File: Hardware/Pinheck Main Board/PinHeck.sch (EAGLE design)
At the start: 363 parts, among them IC2 PIC32MX795F512L-80I/PT, IC3 CD74HCT244E, IC4 CD74HCT244E, IC5 ULN2803A, J11 TC2030-FTDI-TTL-232R, J2 TC2030-FTDI-TTL-232R, J3 N/A, J4 SJ1-2503A, J5 26-64-4020, J9 TC2030-PKT-NL, P1 TC33X-2-103E, U1 P8X32A-Q44, U10 74HCT2G04GV,125, U11 CD74HC165M96, U12 CD74HC165M96, U13 CAT24M01LI-G, U14 MC74HC08ADR2G, U15 MC74HC08ADR2G, U16 MC74HC08ADR2G, U17 MC74HC08ADR2G, U18 MC74HC08ADR2G, U19 MC74HC08ADR2G, U2 DS1340Z-33+, U20 TIP107, U21 TIP107, U22 TIP107, U23 TIP107, U24 TIP107, U25 TIP107, U26 TIP107, U27 TIP107, U28 TIP102, U29 TIP102, U3 CD74HC595M96, U30 TIP102, U31 TIP102, U32 TIP102, U33 TIP102, U34 TIP102, U35 TIP102, U36 WS2801, U37 TIP102, U38 WS2801, U39 NCP1117DT33G, U4 CAT24M01LI-G, U40 TIP102, U41 TIP102, U42 TIP102, U43 TIP102, U44 TIP102, U45 TIP102, U46 TIP102, U47 TIP102, U48 TIP102, U49 TIP102, U5 CD74HC595M96, U50 TIP102, U51 TIP102, U52 CD74HC123M96, U6 TIP102, U7 TIP102, U8 TIP102, U9 TIP102, X1 FQ7050B-8.000, X2 9C-6.500MAAJ-T, X3 ABS25-32.768KHz-1-T

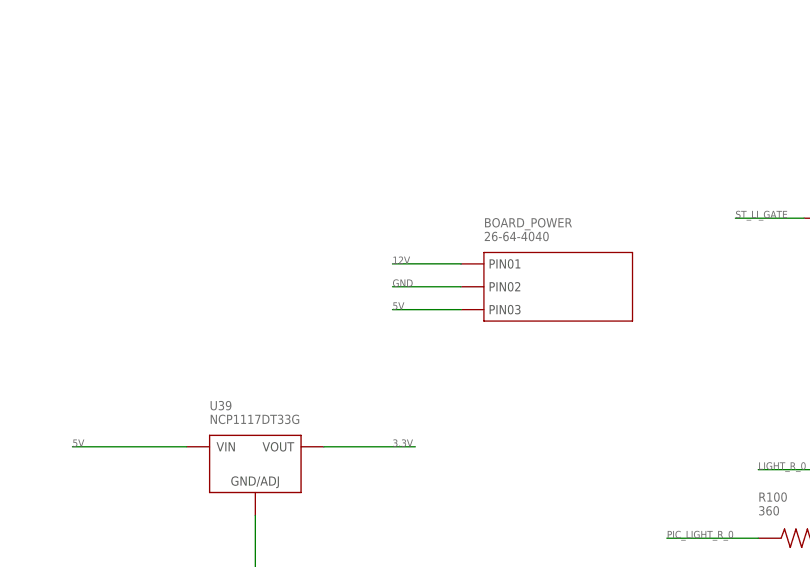
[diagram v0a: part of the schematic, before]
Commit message: Starting layout of parts and connectors
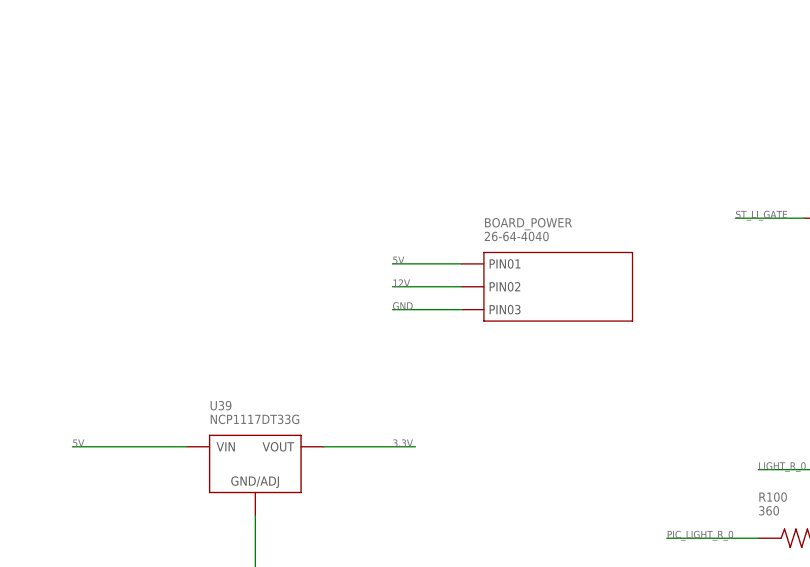
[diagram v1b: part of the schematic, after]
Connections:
- net 12V: now also BOARD_POWER.PIN2; no longer BOARD_POWER.PIN1
- net 5V: now also BOARD_POWER.PIN1; no longer BOARD_POWER.PIN3
- net GND: now also BOARD_POWER.PIN3; no longer BOARD_POWER.PIN2
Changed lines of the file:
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@@
 <grid distance="0.1" unitdist="inch" unit="inch" style="lines" multiple="1" display="no" altdistance="0.01" altunitdist="inch" altunit="inch"/>
 <layers>
-<layer number="1" name="Top" color="4" fill="1" visible="yes" active="no"/>
-<layer number="2" name="Route2" color="1" fill="3" visible="yes" active="no"/>
-<layer number="3" name="Route3" color="4" fill="3" visible="yes" active="no"/>
-<layer number="4" name="Route4" color="1" fill="4" visible="yes" active="no"/>
-<layer number="5" name="Route5" color="4" fill="4" visible="yes" active="no"/>
-<layer number="6" name="Route6" color="1" fill="8" visible="yes" active="no"/>
-<layer number="7" name="Route7" color="4" fill="8" visible="yes" active="no"/>
-<layer number="8" name="Route8" color="1" fill="2" visible="yes" active="no"/>
-<layer number="9" name="Route9" color="4" fill="2" visible="yes" active="no"/>
-<layer number="10" name="Route10" color="1" fill="7" visible="yes" active="no"/>
-<layer number="11" name="Route11" color="4" fill="7" visible="yes" active="no"/>
-<layer number="12" name="Route12" color="1" fill="5" visible="yes" active="no"/>
-<layer number="13" name="Route13" color="4" fill="5" visible="yes" active="no"/>
-<layer number="14" name="Route14" color="1" fill="6" visible="yes" active="no"/>
-<layer number="15" name="Route15" color="4" fill="6" visible="yes" active="no"/>
-<layer number="16" name="Bottom" color="1" fill="1" visible="yes" active="no"/>
-<layer number="17" name="Pads" color="2" fill="1" visible="yes" active="no"/>
-<layer number="18" name="Vias" color="2" fill="1" visible="yes" active="no"/>
-<layer number="19" name="Unrouted" color="6" fill="1" visible="yes" active="no"/>
-<layer number="20" name="Dimension" color="15" fill="1" visible="yes" active="no"/>
-<layer number="21" name="tPlace" color="7" fill="1" visible="yes" active="no"/>
-<layer number="22" name="bPlace" color="7" fill="1" visible="yes" active="no"/>
-<layer number="23" name="tOrigins" color="15" fill="1" visible="yes" active="no"/>
-<layer number="24" name="bOrigins" color="15" fill="1" visible="yes" active="no"/>
-<layer number="25" name="tNames" color="7" fill="1" visible="yes" active="no"/>
-<layer number="26" name="bNames" color="7" fill="1" visible="yes" active="no"/>
-<layer number="27" name="tValues" color="7" fill="1" visible="yes" active="no"/>
-<layer number="28" name="bValues" color="7" fill="1" visible="yes" active="no"/>
+<layer number="1" name="Top" color="4" fill="1" visible="no" active="no"/>
+<layer number="2" name="Route2" color="1" fill="3" visible="no" active="no"/>
+<layer number="3" name="Route3" color="4" fill="3" visible="no" active="no"/>
+<layer number="4" name="Route4" color="1" fill="4" visible="no" active="no"/>
+<layer number="5" name="Route5" color="4" fill="4" visible="no" active="no"/>
+<layer number="6" name="Route6" color="1" fill="8" visible="no" active="no"/>
+<layer number="7" name="Route7" color="4" fill="8" visible="no" active="no"/>
+<layer number="8" name="Route8" color="1" fill="2" visible="no" active="no"/>
+<layer number="9" name="Route9" color="4" fill="2" visible="no" active="no"/>
+<layer number="10" name="Route10" color="1" fill="7" visible="no" active="no"/>
+<layer number="11" name="Route11" color="4" fill="7" visible="no" active="no"/>
+<layer number="12" name="Route12" color="1" fill="5" visible="no" active="no"/>
+<layer number="13" name="Route13" color="4" fill="5" visible="no" active="no"/>
+<layer number="14" name="Route14" color="1" fill="6" visible="no" active="no"/>
+<layer number="15" name="Route15" color="4" fill="6" visible="no" active="no"/>
+<layer number="16" name="Bottom" color="1" fill="1" visible="no" active="no"/>
+<layer number="17" name="Pads" color="2" fill="1" visible="no" active="no"/>
+<layer number="18" name="Vias" color="2" fill="1" visible="no" active="no"/>
+<layer number="19" name="Unrouted" color="6" fill="1" visible="no" active="no"/>
+<layer number="20" name="Dimension" color="15" fill="1" visible="no" active="no"/>
+<layer number="21" name="tPlace" color="7" fill="1" visible="no" active="no"/>
+<layer number="22" name="bPlace" color="7" fill="1" visible="no" active="no"/>
+<layer number="23" name="tOrigins" color="15" fill="1" visible="no" active="no"/>
+<layer number="24" name="bOrigins" color="15" fill="1" visible="no" active="no"/>
+<layer number="25" name="tNames" color="7" fill="1" visible="no" active="no"/>
+<layer number="26" name="bNames" color="7" fill="1" visible="no" active="no"/>
+<layer number="27" name="tValues" color="7" fill="1" visible="no" active="no"/>
+<layer number="28" name="bValues" color="7" fill="1" visible="no" active="no"/>
 <layer number="29" name="tStop" color="7" fill="3" visible="no" active="no"/>
 <layer number="30" name="bStop" color="7" fill="6" visible="no" active="no"/>
@@
 <layer number="35" name="tGlue" color="7" fill="4" visible="no" active="no"/>
 <layer number="36" name="bGlue" color="7" fill="5" visible="no" active="no"/>
-<layer number="37" name="tTest" color="7" fill="1" visible="yes" active="no"/>
-<layer number="38" name="bTest" color="7" fill="1" visible="yes" active="no"/>
+<layer number="37" name="tTest" color="7" fill="1" visible="no" active="no"/>
+<layer number="38" name="bTest" color="7" fill="1" visible="no" active="no"/>
 <layer number="39" name="tKeepout" color="4" fill="11" visible="no" active="no"/>
 <layer number="40" name="bKeepout" color="1" fill="11" visible="no" active="no"/>
@@
 <layer number="44" name="Drills" color="7" fill="1" visible="no" active="no"/>
 <layer number="45" name="Holes" color="7" fill="1" visible="no" active="no"/>
-<layer number="46" name="Milling" color="3" fill="1" visible="yes" active="no"/>
-<layer number="47" name="Measures" color="7" fill="1" visible="yes" active="no"/>
-<layer number="48" name="Document" color="7" fill="1" visible="yes" active="no"/>
-<layer number="49" name="Reference" color="7" fill="1" visible="yes" active="no"/>
-<layer number="50" name="dxf" color="7" fill="1" visible="yes" active="no"/>
-<layer number="51" name="tDocu" color="7" fill="1" visible="yes" active="no"/>
-<layer number="52" name="bDocu" color="7" fill="1" visible="yes" active="no"/>
-<layer number="53" name="tGND_GNDA" color="7" fill="9" visible="yes" active="no"/>
-<layer number="54" name="bGND_GNDA" color="1" fill="9" visible="yes" active="no"/>
-<layer number="56" name="wert" color="7" fill="1" visible="yes" active="no"/>
+<layer number="46" name="Milling" color="3" fill="1" visible="no" active="no"/>
+<layer number="47" name="Measures" color="7" fill="1" visible="no" active="no"/>
+<layer number="48" name="Document" color="7" fill="1" visible="no" active="no"/>
+<layer number="49" name="Reference" color="7" fill="1" visible="no" active="no"/>
+<layer number="50" name="dxf" color="7" fill="1" visible="no" active="no"/>
+<layer number="51" name="tDocu" color="7" fill="1" visible="no" active="no"/>
+<layer number="52" name="bDocu" color="7" fill="1" visible="no" active="no"/>
+<layer number="53" name="tGND_GNDA" color="7" fill="9" visible="no" active="no"/>
+<layer number="54" name="bGND_GNDA" color="1" fill="9" visible="no" active="no"/>
+<layer number="56" name="wert" color="7" fill="1" visible="no" active="no"/>
 <layer number="91" name="Nets" color="2" fill="1" visible="yes" active="yes"/>
 <layer number="92" name="Busses" color="1" fill="1" visible="yes" active="yes"/>
@@
 </segment>
 <segment>
-<wire x1="795.02" y1="182.88" x2="787.4" y2="182.88" width="0.1524" layer="91"/>
-<label x="787.4" y="182.88" size="0.8128" layer="95" font="vector"/>
-<pinref part="BOARD_POWER" gate="G$1" pin="PIN2"/>
-</segment>
-<segment>
 <wire x1="525.78" y1="5.08" x2="518.16" y2="5.08" width="0.1524" layer="91"/>
 <pinref part="C48" gate="G$1" pin="2"/>
@@
 <label x="678.18" y="-73.66" size="0.8128" layer="95" font="vector"/>
 </segment>
+<segment>
+<wire x1="795.02" y1="180.34" x2="787.4" y2="180.34" width="0.1524" layer="91"/>
+<label x="787.4" y="180.34" size="0.8128" layer="95" font="vector"/>
+<pinref part="BOARD_POWER" gate="G$1" pin="PIN3"/>
+</segment>
 </net>
 <net name="RX_PIC32" class="0">
@@
 </segment>
 <segment>
-<wire x1="795.02" y1="180.34" x2="787.4" y2="180.34" width="0.1524" layer="91"/>
-<label x="787.4" y="180.34" size="0.8128" layer="95" font="vector"/>
-<pinref part="BOARD_POWER" gate="G$1" pin="PIN3"/>
-</segment>
-<segment>
 <wire x1="525.78" y1="17.78" x2="518.16" y2="17.78" width="0.1524" layer="91"/>
 <pinref part="C48" gate="G$1" pin="1"/>
@@
 <label x="688.34" y="-58.42" size="0.8128" layer="95" font="vector"/>
 </segment>
+<segment>
+<wire x1="795.02" y1="185.42" x2="787.4" y2="185.42" width="0.1524" layer="91"/>
+<label x="787.4" y="185.42" size="0.8128" layer="95" font="vector"/>
+<pinref part="BOARD_POWER" gate="G$1" pin="PIN1"/>
+</segment>
 </net>
 <net name="DATA_LAT" class="0">
@@
 </segment>
 <segment>
-<wire x1="795.02" y1="185.42" x2="787.4" y2="185.42" width="0.1524" layer="91"/>
-<label x="787.4" y="185.42" size="0.8128" layer="95" font="vector"/>
-<pinref part="BOARD_POWER" gate="G$1" pin="PIN1"/>
-</segment>
-<segment>
 <pinref part="J7" gate="G$1" pin="PIN1"/>
 <wire x1="914.4" y1="40.64" x2="901.7" y2="40.64" width="0.1524" layer="91"/>
 <label x="901.7" y="40.64" size="0.8128" layer="95" font="vector"/>
 </segment>
+<segment>
+<wire x1="795.02" y1="182.88" x2="787.4" y2="182.88" width="0.1524" layer="91"/>
+<label x="787.4" y="182.88" size="0.8128" layer="95" font="vector"/>
+<pinref part="BOARD_POWER" gate="G$1" pin="PIN2"/>
+</segment>
 </net>

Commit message: Layout of parts almost done. Needs some tweaking but everything fits.
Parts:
- PIC32_UART: LABEL01 (none) -> GND; LABEL04 (none) -> RX_PIC32; LABEL05 (none) -> TX_PIC32; LABEL06 (none) -> !RST!_PIC32
- PROP_UART: LABEL01 (none) -> GND; LABEL04 (none) -> RX_PROP; LABEL05 (none) -> TX_PROP; LABEL06 (none) -> !RES!_PROP
- renumbered J1 to PROP_UART, J10 to PIC32_UART, J11 to PIC32_TC, J2 to PROP_TC, J8 to PICKIT3, J9 to PICKIT3_TC, SW1 to PIC_RST, SW3 to PIC_PROGRAM

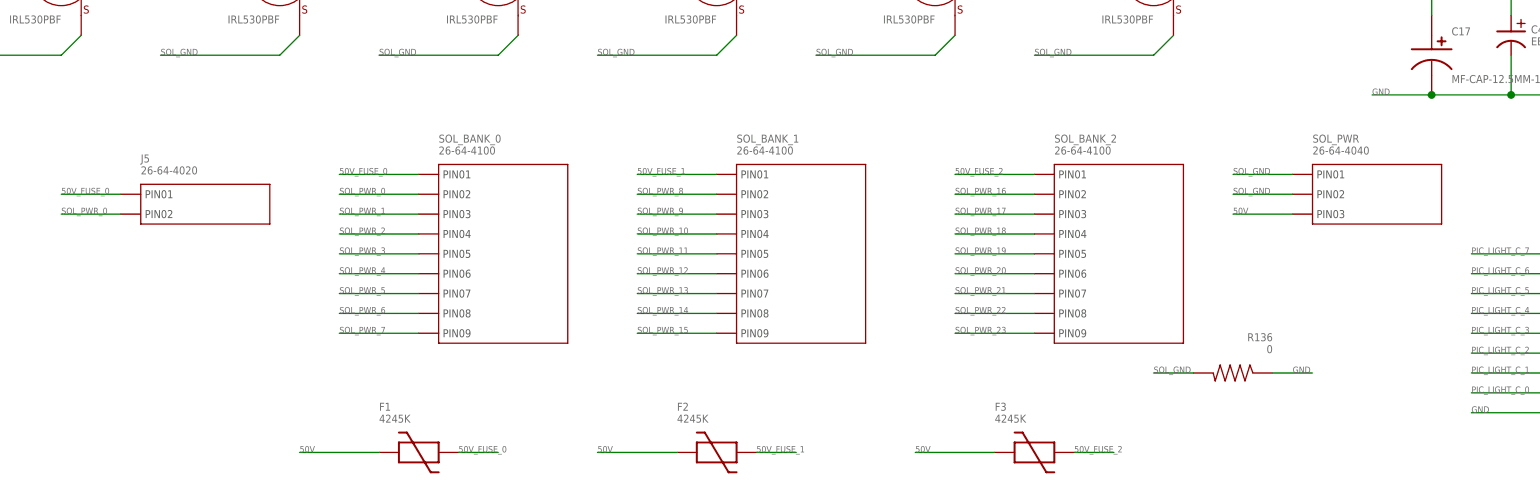
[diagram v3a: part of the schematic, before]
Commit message: Routing the solenoid power area.
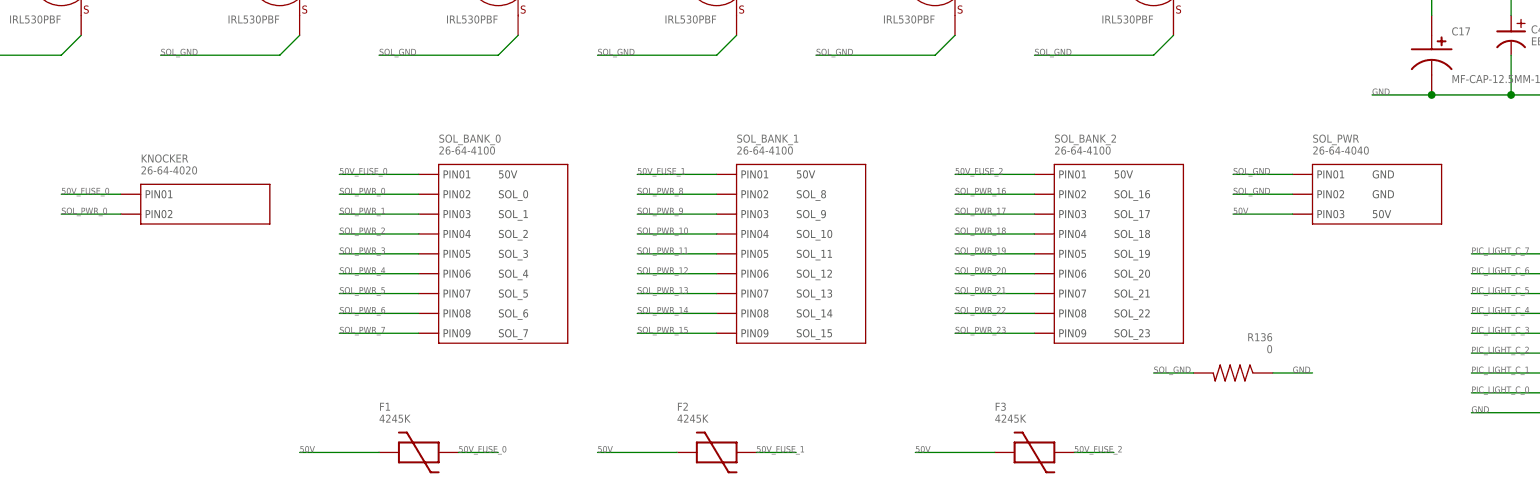
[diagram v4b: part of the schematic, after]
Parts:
- SOL_BANK_0: LABEL01 (none) -> 50V; LABEL02 (none) -> SOL_0; LABEL03 (none) -> SOL_1; LABEL04 (none) -> SOL_2; LABEL05 (none) -> SOL_3; LABEL06 (none) -> SOL_4; LABEL07 (none) -> SOL_5; LABEL08 (none) -> SOL_6; LABEL09 (none) -> SOL_7
- SOL_BANK_1: LABEL01 (none) -> 50V; LABEL02 (none) -> SOL_8; LABEL03 (none) -> SOL_9; LABEL04 (none) -> SOL_10; LABEL05 (none) -> SOL_11; LABEL06 (none) -> SOL_12; LABEL07 (none) -> SOL_13; LABEL08 (none) -> SOL_14; LABEL09 (none) -> SOL_15
- SOL_BANK_2: LABEL01 (none) -> 50V; LABEL02 (none) -> SOL_16; LABEL03 (none) -> SOL_17; LABEL04 (none) -> SOL_18; LABEL05 (none) -> SOL_19; LABEL06 (none) -> SOL_20; LABEL07 (none) -> SOL_21; LABEL08 (none) -> SOL_22; LABEL09 (none) -> SOL_23
- SOL_PWR: LABEL01 (none) -> GND; LABEL02 (none) -> GND; LABEL03 (none) -> 50V
- renumbered J5 to KNOCKER
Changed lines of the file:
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@@
 <part name="R137" library="PP_Passives" deviceset="RESISTOR" device="_0805" value="10K"/>
 <part name="U$2" library="PP_Aesthetics" deviceset="MF_LOGO" device="LOGO_TEXT"/>
-<part name="SOL_BANK_0" library="PP_Connectors" deviceset="CON_01X09" device="_26-64-4100_(KEYPIN6)" value="26-64-4100"/>
-<part name="SOL_BANK_1" library="PP_Connectors" deviceset="CON_01X09" device="_26-64-4100_(KEYPIN7)" value="26-64-4100"/>
-<part name="SOL_BANK_2" library="PP_Connectors" deviceset="CON_01X09" device="_26-64-4100_(KEYPIN8)" value="26-64-4100"/>
+<part name="SOL_BANK_0" library="PP_Connectors" deviceset="CON_01X09" device="_26-64-4100_(KEYPIN6)" value="26-64-4100">
+<attribute name="LABEL01" value="50V"/>
+<attribute name="LABEL02" value="SOL_0"/>
+<attribute name="LABEL03" value="SOL_1"/>
+<attribute name="LABEL04" value="SOL_2"/>
+<attribute name="LABEL05" value="SOL_3"/>
+<attribute name="LABEL06" value="SOL_4"/>
+<attribute name="LABEL07" value="SOL_5"/>
+<attribute name="LABEL08" value="SOL_6"/>
+<attribute name="LABEL09" value="SOL_7"/>
+</part>
+<part name="SOL_BANK_1" library="PP_Connectors" deviceset="CON_01X09" device="_26-64-4100_(KEYPIN7)" value="26-64-4100">
+<attribute name="LABEL01" value="50V"/>
+<attribute name="LABEL02" value="SOL_8"/>
+<attribute name="LABEL03" value="SOL_9"/>
+<attribute name="LABEL04" value="SOL_10"/>
+<attribute name="LABEL05" value="SOL_11"/>
+<attribute name="LABEL06" value="SOL_12"/>
+<attribute name="LABEL07" value="SOL_13"/>
+<attribute name="LABEL08" value="SOL_14"/>
+<attribute name="LABEL09" value="SOL_15"/>
+</part>
+<part name="SOL_BANK_2" library="PP_Connectors" deviceset="CON_01X09" device="_26-64-4100_(KEYPIN8)" value="26-64-4100">
+<attribute name="LABEL01" value="50V"/>
+<attribute name="LABEL02" value="SOL_16"/>
+<attribute name="LABEL03" value="SOL_17"/>
+<attribute name="LABEL04" value="SOL_18"/>
+<attribute name="LABEL05" value="SOL_19"/>
+<attribute name="LABEL06" value="SOL_20"/>
+<attribute name="LABEL07" value="SOL_21"/>
+<attribute name="LABEL08" value="SOL_22"/>
+<attribute name="LABEL09" value="SOL_23"/>
+</part>
 <part name="SW_ROW" library="PP_Connectors" deviceset="CON_01X09" device="_26-64-4100_(KEYPIN4)" value="26-64-4100"/>
 <part name="SW_COL" library="PP_Connectors" deviceset="CON_01X09" device="_26-64-4100_(KEYPIN5)" value="26-64-4100"/>
@@
 <part name="U4" library="PP_DigitalIC" deviceset="EEPROM_I2C" device="DIP-8" value="CAT24M01LI-G"/>
 <part name="BOARD_POWER" library="PP_Connectors" deviceset="CON_01X03" device="_26-64-4040_(KEYPIN2)" value="26-64-4040"/>
-<part name="SOL_PWR" library="PP_Connectors" deviceset="CON_01X03" device="_26-64-4040_(KEYPIN3)" value="26-64-4040"/>
+<part name="SOL_PWR" library="PP_Connectors" deviceset="CON_01X03" device="_26-64-4040_(KEYPIN3)" value="26-64-4040">
+<attribute name="LABEL01" value="GND"/>
+<attribute name="LABEL02" value="GND"/>
+<attribute name="LABEL03" value="50V"/>
+</part>
 <part name="U1" library="PP_DigitalIC" deviceset="P8X32A" device="-Q44" value="P8X32A-Q44"/>
 <part name="DMD_CON" library="PP_Connectors" deviceset="CON_02X07" device="_5103308-2" value="5103308-2"/>
@@
 <part name="J7" library="PP_Connectors" deviceset="CON_01X03" device="_26-64-4040_(KEYPIN1)"/>
 <part name="CABINET" library="PP_Connectors" deviceset="CON_01X11" device="_26-64-4120(KEYPIN2)" value="26-64-4120"/>
-<part name="J5" library="PP_Connectors" deviceset="CON_01X02" device="_26-64-4020" value="26-64-4020"/>
+<part name="KNOCKER" library="PP_Connectors" deviceset="CON_01X02" device="_26-64-4020" value="26-64-4020"/>
 <part name="PICKIT3" library="PP_Connectors" deviceset="CON_01X06" device="_2.54MM_PIN_HEADER"/>
 <part name="R24" library="PP_Passives" deviceset="RESISTOR" device="_0805" value="10K"/>
@@
 <instance part="J7" gate="G$1" x="916.94" y="40.64"/>
 <instance part="CABINET" gate="G$1" x="518.16" y="86.36"/>
-<instance part="J5" gate="G$1" x="581.66" y="81.28"/>
+<instance part="KNOCKER" gate="G$1" x="581.66" y="81.28"/>
 <instance part="PICKIT3" gate="G$1" x="15.24" y="106.68"/>
 <instance part="R24" gate="G$1" x="350.52" y="213.36" rot="R90"/>
@@
 <wire x1="571.5" y1="81.28" x2="579.12" y2="81.28" width="0.1524" layer="91"/>
 <label x="571.5" y="81.28" size="0.8128" layer="95" font="vector"/>
-<pinref part="J5" gate="G$1" pin="PIN1"/>
+<pinref part="KNOCKER" gate="G$1" pin="PIN1"/>
 </segment>
 </net>
@@
 <wire x1="579.12" y1="78.74" x2="571.5" y2="78.74" width="0.1524" layer="91"/>
 <label x="571.5" y="78.74" size="0.8128" layer="95" font="vector"/>
-<pinref part="J5" gate="G$1" pin="PIN2"/>
+<pinref part="KNOCKER" gate="G$1" pin="PIN2"/>
 </segment>
 <segment>

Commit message: Added changes for Ben
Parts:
- U37: value TIP102 -> TIP107; device PP_DiscreteSemi:BJT_NPN_SINGLE_TO-220 -> PP_DiscreteSemi:BJT_PNP_SINGLE_TO-220
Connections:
- net AC_17 renamed SERVO_2
- net AC_33 renamed SERVO_4
- net AC_34 renamed SERVO_3
- net AC_44 renamed SERVO_1
- net AC_46 renamed SERVO_0
- net COMM_ATN renamed COMM_IN_TX
- net COMM_CLK renamed COMM_CLK_RX
- net COMM_DATA renamed COMM_OUT
- net DATA_CAB renamed CAB_SWITCH_IN
- net DATA_CLK renamed CAB_CLK
- net DATA_LAT renamed CAB_LAT
- net GI_DATA_COL renamed CAB_GI_OUT
- net MENU renamed BACK
- net RG9 renamed PIC_PROGRAM_SW
- removed net RC1: IC2PC.T2CK/RC1
- removed net RG6: IC2PG.ECOL/SCK2A/U2BTXU2ARTS/PMA5/CN8/RG6
- new net EXT_RGB_CLK: IC2PC.T2CK/RC1, RGB_COM_OUT.3
- new net EXT_RGB_DATA: IC2PG.ECOL/SCK2A/U2BTXU2ARTS/PMA5/CN8/RG6, RGB_COM_OUT.2
- net 5V: now also R115.1, U37.EMITTER
- net GND: no longer R115.1, U37.EMITTER
- net RGB_CLK_OUT: no longer RGB_COM_OUT.3
- net RGB_DATA_OUT: no longer RGB_COM_OUT.2
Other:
- moved on the sheet: R115, U37
